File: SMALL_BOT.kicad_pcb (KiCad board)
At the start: 2 copper layers, 80 x 65 mm, 37 parts, among them J1 MOTOR_B, J10 JMP, J11 UART, J12 LEDS, J13 I2C, J14 LEDS, J15 HEADER_1, J16 HEADER_1, J2 MOTOR_A, J3 HEADER_1, J4 HEADER_1, J5 HC-SR04, J6 HC-SR04, J7 HC-SR04, J8 HC-SR04, J9 Bateria, Q1 2N7002, U1 Teensy4.0_B, U2 DRV8872, U3 LM1117-SOT, U4 DRV8872

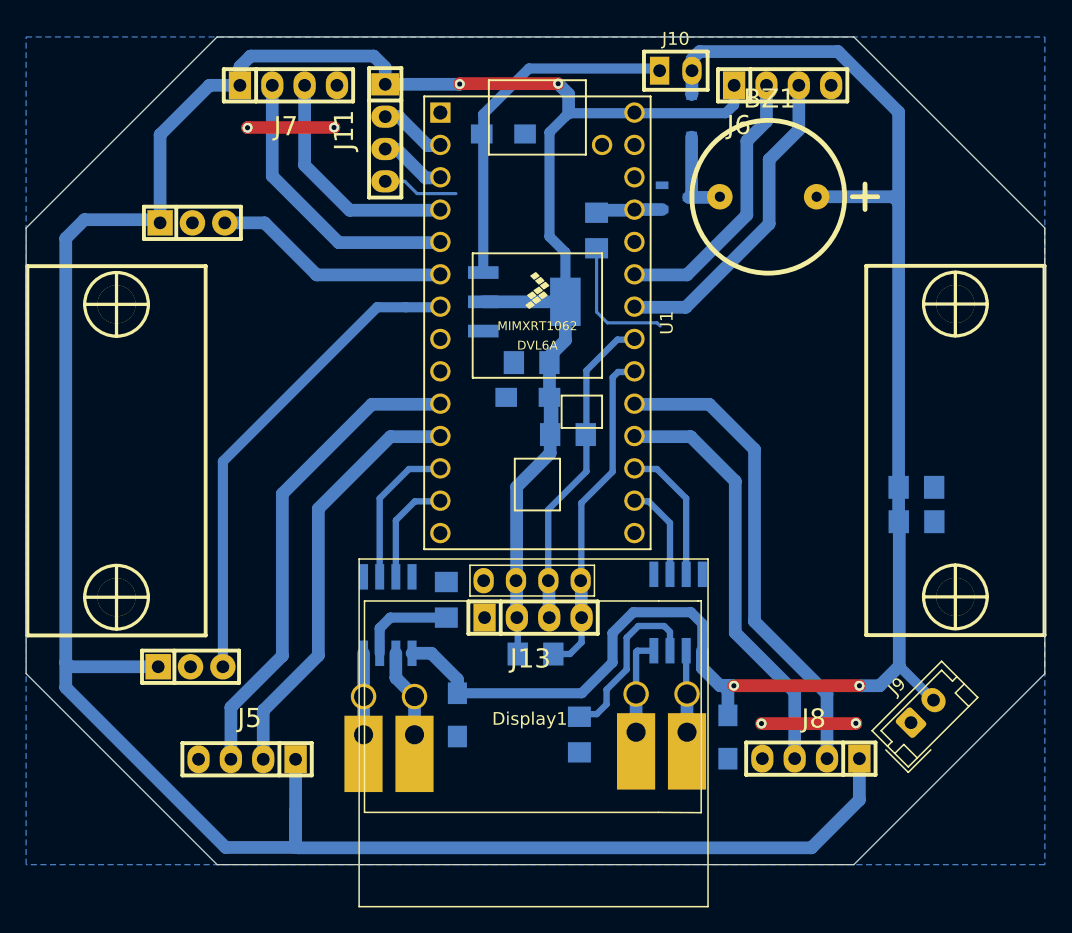
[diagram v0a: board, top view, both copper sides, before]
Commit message: se agrego pinout del robot
se modifico serigrafia y se agrego pinout
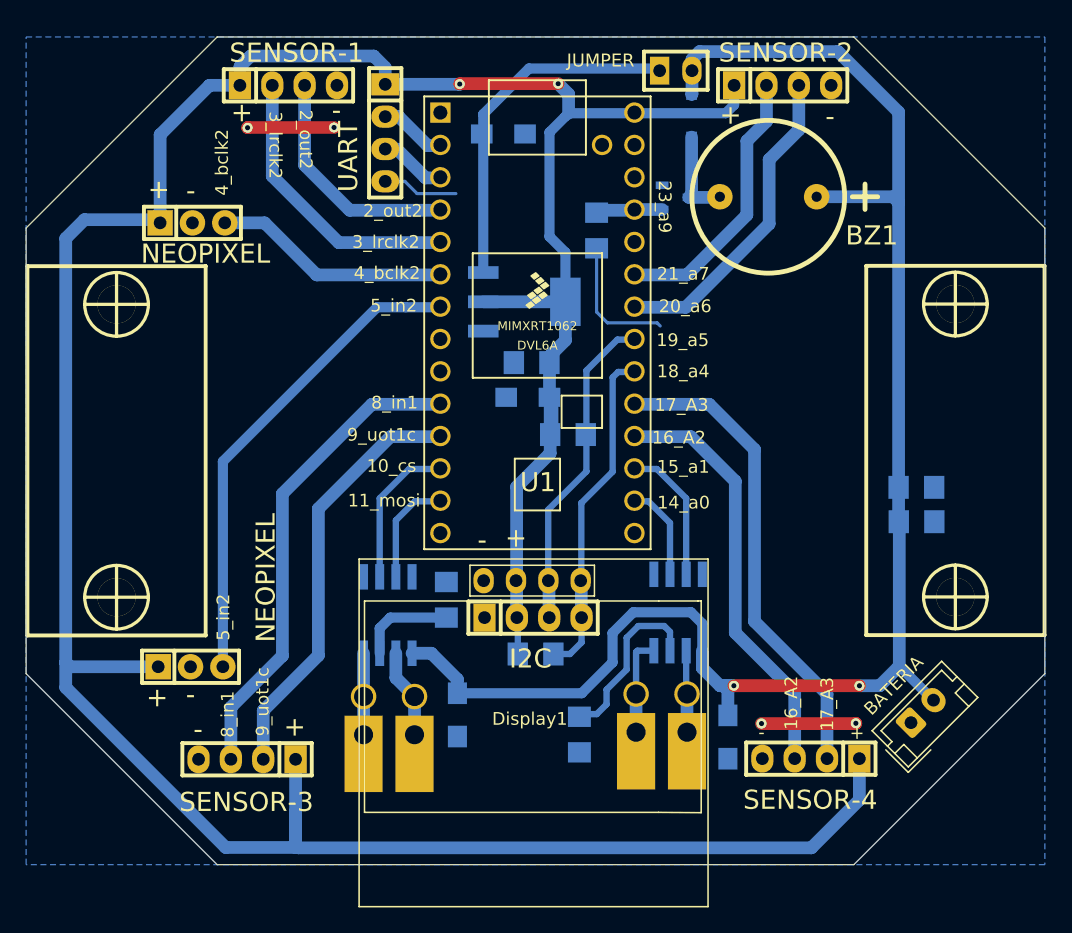
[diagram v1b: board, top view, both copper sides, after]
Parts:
- renumbered J9 to BATERIA, J13 to I2C, J10 to JUMPER, J7 to SENSOR-1, J6 to SENSOR-2, J5 to SENSOR-3, J8 to SENSOR-4, J11 to UART
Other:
- board text added: "+"
- board text added: "-"
- board text added: "10_cs"
- board text added: "11_mosi"
- board text added: "14_a0"
- board text added: "15_a1"
- board text added: "16_A2"
- board text added: "17_A3"
- board text added: "18_a4"
- board text added: "19_a5"
- board text added: "20_a6"
- board text added: "21_a7"
- board text added: "23_a9"
- board text added: "2_out2"
- board text added: "3_lrclk2"
- board text added: "4_bclk2"
- board text added: "5_in2"
- board text added: "8_in1"
- board text added: "9_uot1c"
- board text added: "NEOPIXEL"

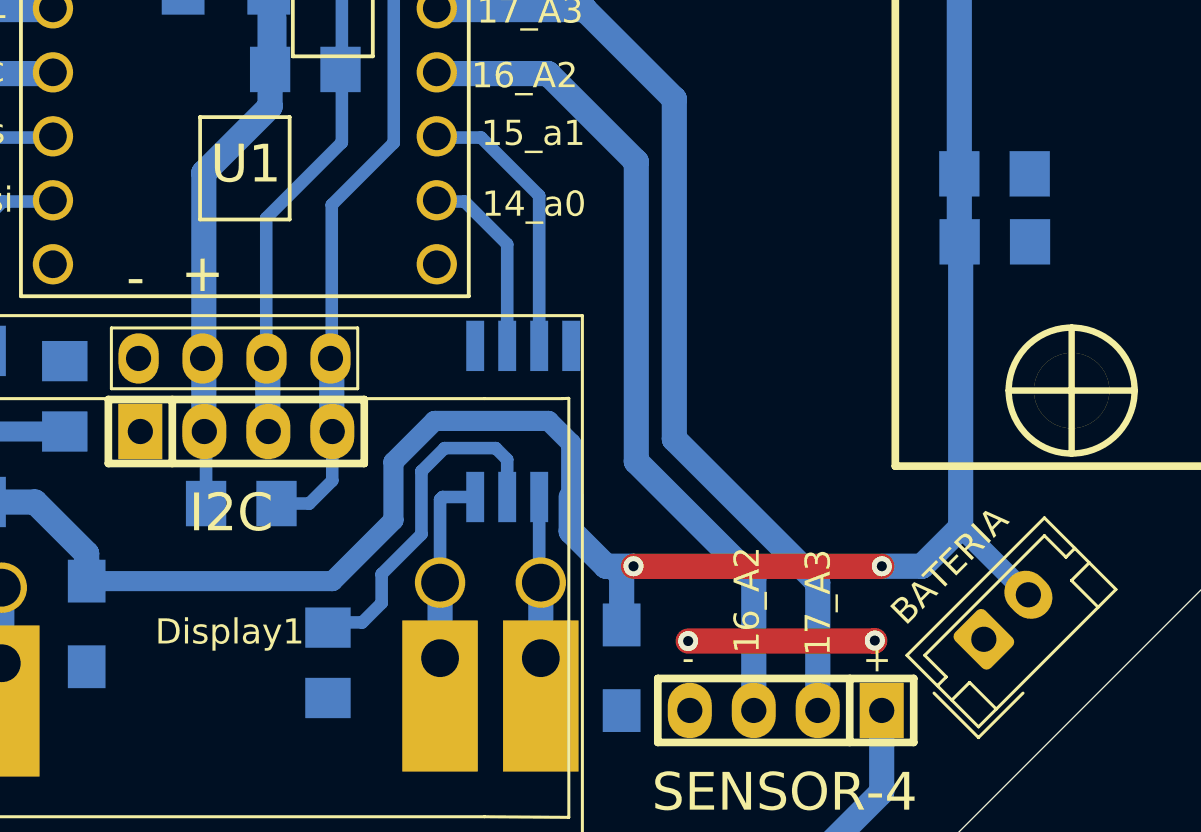
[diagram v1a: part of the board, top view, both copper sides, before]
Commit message: SCH y capacitores
Genera la version inicial del SCH en pdf y  cambie de posición 2 capacitores SMD que estaban debajo de uno de los motores.
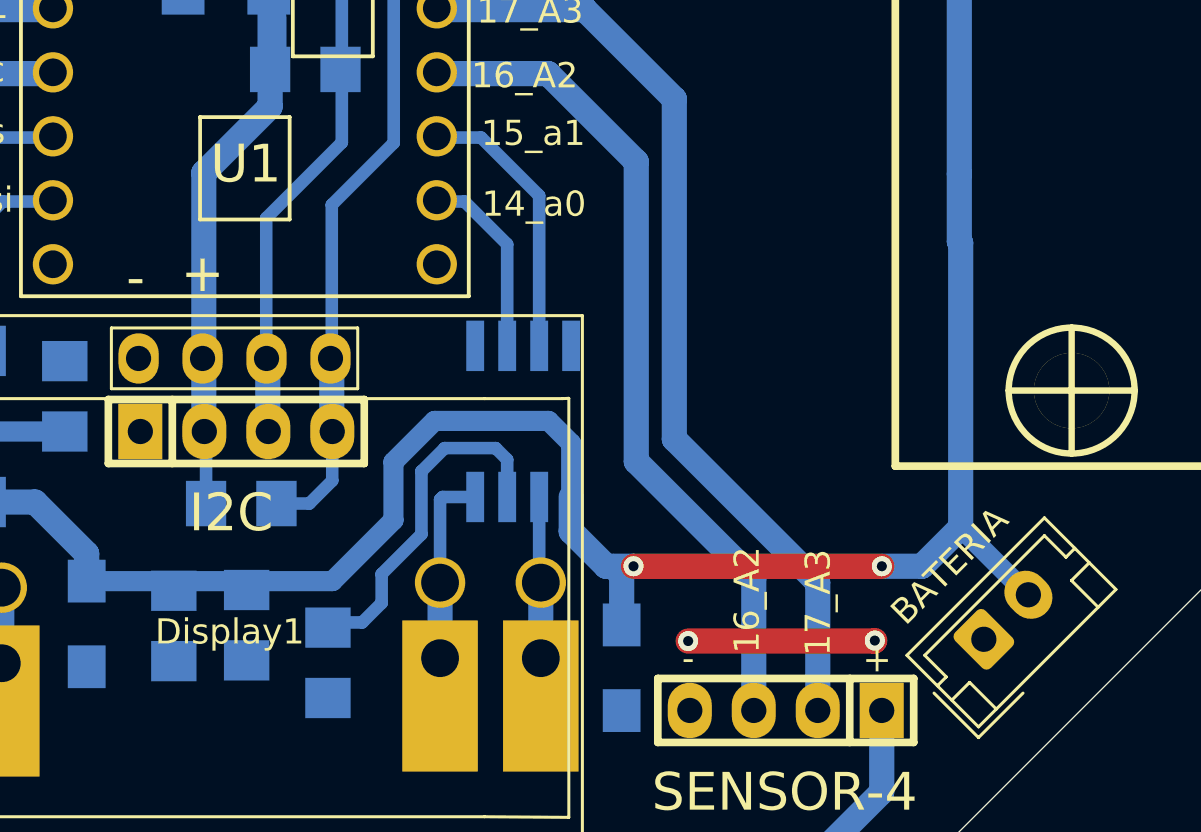
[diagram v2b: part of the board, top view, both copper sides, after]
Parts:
- moved C6 37.2 mm to (117.3, 138.3), turned to 90 degrees
- moved C4 33.4 mm to (120.2, 138.3), turned to 90 degrees

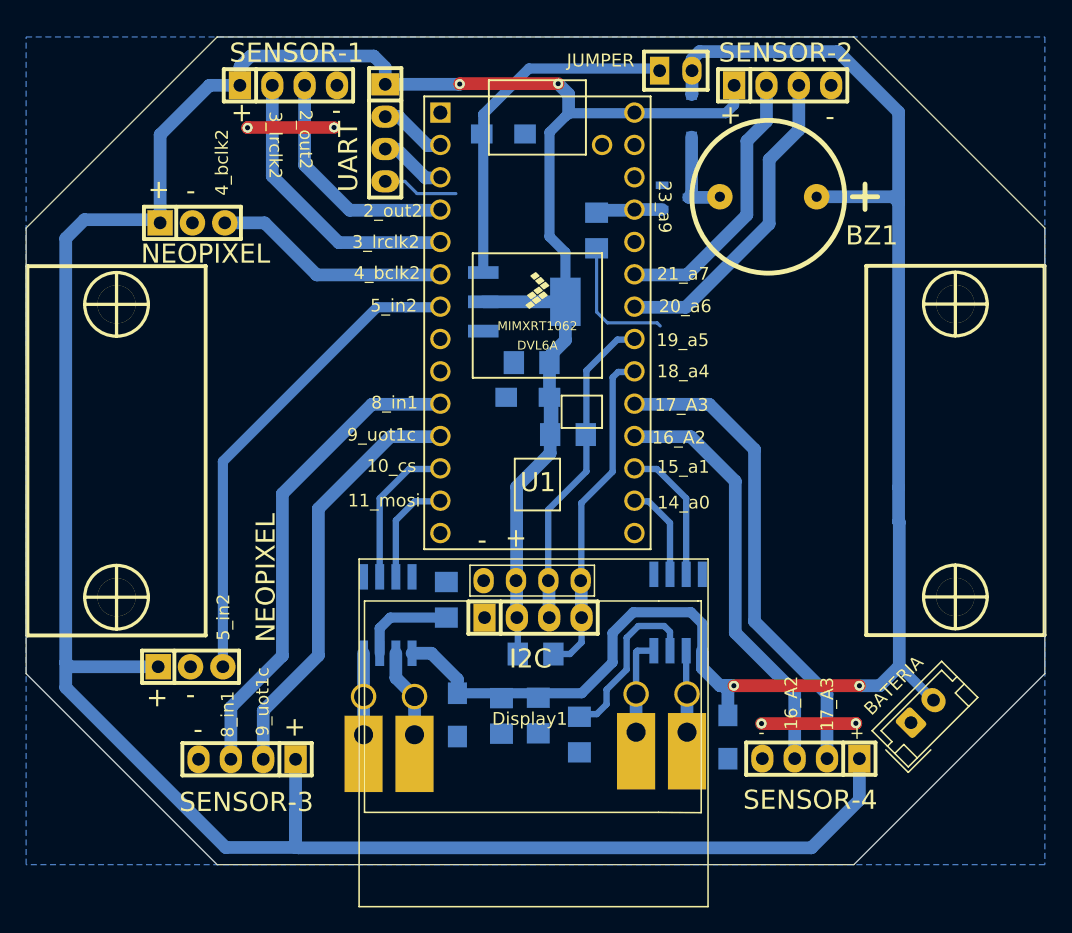
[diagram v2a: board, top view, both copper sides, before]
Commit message: modificaciones
se cambio 5v a 3v3, se movieron los capacitores de los drivers de motores
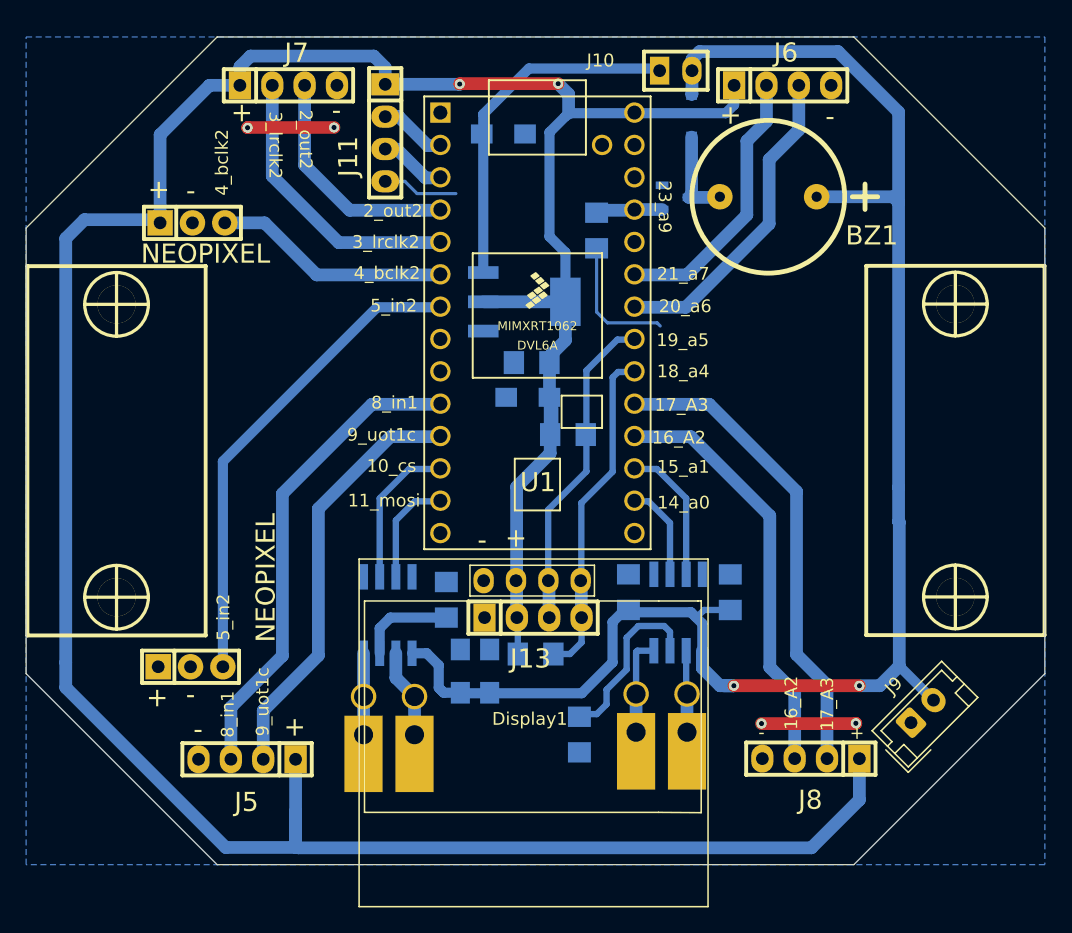
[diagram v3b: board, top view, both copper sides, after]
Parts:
- moved C6 20.4 mm to (135.3, 128.6), turned to 270 degrees
- moved C7 19.4 mm to (116.4, 134.8), turned to 90 degrees
- moved C4 12.0 mm to (127.3, 128.6), turned to 270 degrees
- moved C5 3.45 mm to (114.1, 134.8), turned to 90 degrees
- renumbered JUMPER to J10, UART to J11, I2C to J13, SENSOR-3 to J5, SENSOR-2 to J6, SENSOR-1 to J7, SENSOR-4 to J8, BATERIA to J9
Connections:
- C2 pad 1: +5V -> +3V3
- C3 pad 1: +5V -> +3V3
- Display1 pad 2: +5V -> +3V3
- J11 pad 1: +5V -> +3V3
- J12 pad 1: +5V -> +3V3
- J13 pad 2: +5V -> +3V3
- J14 pad 1: +5V -> (no net)
- J5 pad 1: +5V -> +3V3
- J6 pad 1: +5V -> +3V3
- J7 pad 1: +5V -> +3V3
- J8 pad 1: +5V -> +3V3
- R4 pad 1: +5V -> +3V3
- R5 pad 1: +5V -> +3V3
- U1 pad 33: +5V -> +3V3
- U3 pad 2: +5V -> +3V3
- U3 pad 4: +5V -> +3V3
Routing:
- net +5V: track 247.5 -> 0.00 mm, vias 2 -> 0
- net +3V3: track 0.00 -> 240.1 mm, vias 0 -> 2
- net /VIN: track 127.9 -> 130.1 mm
